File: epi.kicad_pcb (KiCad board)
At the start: 4 copper layers, 12.7 x 22.8 mm, 31 parts, among them J1 Connector 1x12, J2 Connector 1x12, J3 Conn_01x05, J4 USB-C 2.0 mid-mount female co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, U1 ATmega32U4-M, Y1 Crystal_GND24

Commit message: minor changes
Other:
- outline, holes or cut-outs redrawn
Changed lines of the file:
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@@
     )
     (pad_to_mask_clearance 0)
+    (grid_origin 108.895036 55.708644)
     (pcbplotparams
       (layerselection 0x00010fc_ffffffff)
@@
   (net 41 "D12")
   (net 42 "D13")
-  (net 43 "Net-(J4-PadA4)")
+  (net 43 "Net-(FB1-Pad1)")
   (net 44 "Net-(D2-Pad2)")
   (net 45 "Net-(F1-Pad1)")
@@
       (net 2 "GND") (pintype "passive"))
     (pad "2" smd roundrect (at 0.51 0 90) (size 0.54 0.64) (layers "F.Cu" "F.Paste" "F.Mask") (roundrect_rratio 0.25)
-      (net 43 "Net-(J4-PadA4)") (pintype "passive"))
+      (net 43 "Net-(FB1-Pad1)") (pintype "passive"))
     (model "${KICAD6_3DMODEL_DIR}/Resistor_SMD.3dshapes/R_0402_1005Metric.wrl"
       (offset (xyz 0 0 0))
@@
     (fp_line (start -0.525 -0.27) (end 0.525 -0.27) (layer "F.Fab") (width 0.1))
     (pad "1" smd roundrect (at -0.51 0 90) (size 0.54 0.64) (layers "F.Cu" "F.Paste" "F.Mask") (roundrect_rratio 0.25)
-      (net 43 "Net-(J4-PadA4)") (pintype "passive"))
+      (net 43 "Net-(FB1-Pad1)") (pintype "passive"))
     (pad "2" smd roundrect (at 0.51 0 90) (size 0.54 0.64) (layers "F.Cu" "F.Paste" "F.Mask") (roundrect_rratio 0.25)
       (net 45 "Net-(F1-Pad1)") (pintype "passive"))
@@
       (effects (font (size 1 1) (thickness 0.15)))
     )
-    (fp_rect (start 3 -4.5) (end 3.4 -3.5) (layer "F.Paste") (width 0) (fill solid))
     (pad "A1" smd rect locked (at -3.2 -4 270) (size 1 0.6155) (layers "F.Cu" "F.Paste" "F.Mask")
       (net 2 "GND") (pinfunction "GND") (pintype "passive"))
-    (pad "A1" smd rect locked (at 3.2 -4 270) (size 1 0.6155) (layers "F.Cu" "F.Mask")
+    (pad "A1" smd rect locked (at 3.2 -4 270) (size 1 0.6155) (layers "F.Cu" "F.Paste" "F.Mask")
       (net 2 "GND") (pinfunction "GND") (pintype "passive"))
     (pad "A4" smd rect locked (at -2.4 -4 270) (size 1 0.6155) (layers "F.Cu" "F.Paste" "F.Mask")
-      (net 43 "Net-(J4-PadA4)") (pinfunction "VBUS") (pintype "passive"))
+      (net 43 "Net-(FB1-Pad1)") (pinfunction "VBUS") (pintype "passive"))
     (pad "A5" smd rect locked (at -1.250923 -4 270) (size 1 0.30775) (layers "F.Cu" "F.Paste" "F.Mask")
       (net 11 "Net-(J4-PadA5)") (pinfunction "CC1") (pintype "bidirectional"))
@@
       (net 13 "Net-(J4-PadA7)") (pinfunction "D-") (pintype "bidirectional"))
     (pad "A9" smd rect locked (at 2.4 -4 270) (size 1 0.6155) (layers "F.Cu" "F.Paste" "F.Mask")
-      (net 43 "Net-(J4-PadA4)") (pinfunction "VBUS") (pintype "passive"))
+      (net 43 "Net-(FB1-Pad1)") (pinfunction "VBUS") (pintype "passive"))
     (pad "B5" smd rect locked (at 1.752189 -4 270) (size 1 0.30775) (layers "F.Cu" "F.Paste" "F.Mask")
       (net 14 "Net-(J4-PadB5)") (pinfunction "CC2") (pintype "bidirectional"))
@@
   (gr_line (start 110.69 51.4) (end 110.69 53.65) (layer "Edge.Cuts") (width 0.1))
   (gr_line (start 97.99 51.4) (end 97.99 53.65) (layer "Edge.Cuts") (width 0.1))
-  (gr_line (start 99.64 57.3365) (end 100.84 56.8365) (layer "Edge.Cuts") (width 0.1))
+  (gr_line (start 99.77322 51.4) (end 99.77322 55.708644) (layer "Edge.Cuts") (width 0.1))
   (gr_line (start 100.84 56.8365) (end 107.84 56.8365) (layer "Edge.Cuts") (width 0.1))
   (gr_arc (start 110.69 55.65) (mid 109.69 54.65) (end 110.69 53.65) (layer "Edge.Cuts") (width 0.1))
   (gr_arc (start 97.99 53.65) (mid 98.99 54.65) (end 97.99 55.65) (layer "Edge.Cuts") (width 0.1))
-  (gr_line (start 109.04 51.4) (end 110.69 51.4) (layer "Edge.Cuts") (width 0.1))
-  (gr_line (start 109.04 57.3365) (end 109.04 51.4) (layer "Edge.Cuts") (width 0.1))
+  (gr_arc (start 108.895036 55.708644) (mid 108.814317 56.690524) (end 107.84 56.8365) (layer "Edge.Cuts") (width 0.1))
+  (gr_line (start 108.895036 51.4) (end 110.69 51.4) (layer "Edge.Cuts") (width 0.1))
+  (gr_line (start 108.895036 55.708644) (end 108.895036 51.4) (layer "Edge.Cuts") (width 0.1))
   (gr_line (start 110.69 74.16) (end 110.69 55.65) (layer "Edge.Cuts") (width 0.1))
   (gr_line (start 97.99 74.16) (end 110.69 74.16) (layer "Edge.Cuts") (width 0.1))
   (gr_line (start 97.99 55.65) (end 97.99 74.16) (layer "Edge.Cuts") (width 0.1))
-  (gr_line (start 97.99 51.4) (end 99.64 51.4) (layer "Edge.Cuts") (width 0.1))
-  (gr_line (start 99.64 51.4) (end 99.64 57.3365) (layer "Edge.Cuts") (width 0.1))
-  (gr_line (start 107.84 56.8365) (end 109.04 57.3365) (layer "Edge.Cuts") (width 0.1))
+  (gr_line (start 97.99 51.4) (end 99.77322 51.4) (layer "Edge.Cuts") (width 0.1))
+  (gr_arc (start 100.828256 56.8365) (mid 99.853938 56.690524) (end 99.77322 55.708644) (layer "Edge.Cuts") (width 0.1))
   (gr_text "A1" (at 109.09 66.613) (layer "B.SilkS")
     (effects (font (size 0.8 0.8) (thickness 0.16)) (justify mirror))
@@
   (via (at 103.549883 66.991639) (size 0.6) (drill 0.2) (layers "F.Cu" "B.Cu") (net 2))
   (via (at 101.179122 69.620878) (size 0.6) (drill 0.2) (layers "F.Cu" "B.Cu") (free) (net 2))
-  (segment (start 102.34 68.319037) (end 103 67.659037) (width 0.15) (layer "F.Cu") (net 3))
+  (segment (start 103 67.659037) (end 103 66.782037) (width 0.15) (layer "F.Cu") (net 3))
+  (segment (start 104.8 65.2) (end 105.691356 64.308644) (width 0.15) (layer "F.Cu") (net 3))
+  (segment (start 105.691356 64.308644) (end 106.248706 64.308644) (width 0.15) (layer "F.Cu") (net 3))
+  (segment (start 103 66.782037) (end 103.115 66.667037) (width 0.15) (layer "F.Cu") (net 3))
+  (segment (start 108.535 63.45) (end 108.93 63.45) (width 0.15) (layer "F.Cu") (net 3))
+  (segment (start 103.115 66.667037) (end 103.115 65.445815) (width 0.15) (layer "F.Cu") (net 3))
+  (segment (start 106.87085 63.6865) (end 107.6775 63.6865) (width 0.15) (layer "F.Cu") (net 3))
   (segment (start 102.34 69.524) (end 102.34 68.319037) (width 0.15) (layer "F.Cu") (net 3))
-  (segment (start 108.535 63.45) (end 108.93 63.45) (width 0.15) (layer "F.Cu") (net 3))
-  (segment (start 104.8 65.2) (end 105.6 64.4) (width 0.15) (layer "F.Cu") (net 3))
-  (segment (start 106.87085 63.6865) (end 107.6775 63.6865) (width 0.15) (layer "F.Cu") (net 3))
-  (segment (start 105.6 64.4) (end 106.15735 64.4) (width 0.15) (layer "F.Cu") (net 3))
-  (segment (start 103 67.659037) (end 103 66.782037) (width 0.15) (layer "F.Cu") (net 3))
-  (segment (start 103 66.782037) (end 103.115 66.667037) (width 0.15) (layer "F.Cu") (net 3))
+  (segment (start 103.360815 65.2) (end 104.8 65.2) (width 0.15) (layer "F.Cu") (net 3))
+  (segment (start 103.115 65.445815) (end 103.360815 65.2) (width 0.15) (layer "F.Cu") (net 3))
   (segment (start 108.2985 63.6865) (end 108.535 63.45) (width 0.15) (layer "F.Cu") (net 3))
   (segment (start 107.6775 63.6865) (end 108.2985 63.6865) (width 0.15) (layer "F.Cu") (net 3))
   (segment (start 108.92 63.46) (end 108.93 63.45) (width 0.15) (layer "F.Cu") (net 3))
-  (segment (start 103.360815 65.2) (end 104.8 65.2) (width 0.15) (layer "F.Cu") (net 3))
-  (segment (start 103.115 66.667037) (end 103.115 65.445815) (width 0.15) (layer "F.Cu") (net 3))
-  (segment (start 106.15735 64.4) (end 106.87085 63.6865) (width 0.15) (layer "F.Cu") (net 3))
-  (segment (start 103.115 65.445815) (end 103.360815 65.2) (width 0.15) (layer "F.Cu") (net 3))
+  (segment (start 106.248706 64.308644) (end 106.87085 63.6865) (width 0.15) (layer "F.Cu") (net 3))
+  (segment (start 102.34 68.319037) (end 103 67.659037) (width 0.15) (layer "F.Cu") (net 3))
   (segment (start 108.92 64.32) (end 108.92 63.46) (width 0.15) (layer "F.Cu") (net 3))
   (segment (start 104.4 61.08) (end 103.87 60.55) (width 0.2) (layer "F.Cu") (net 4))

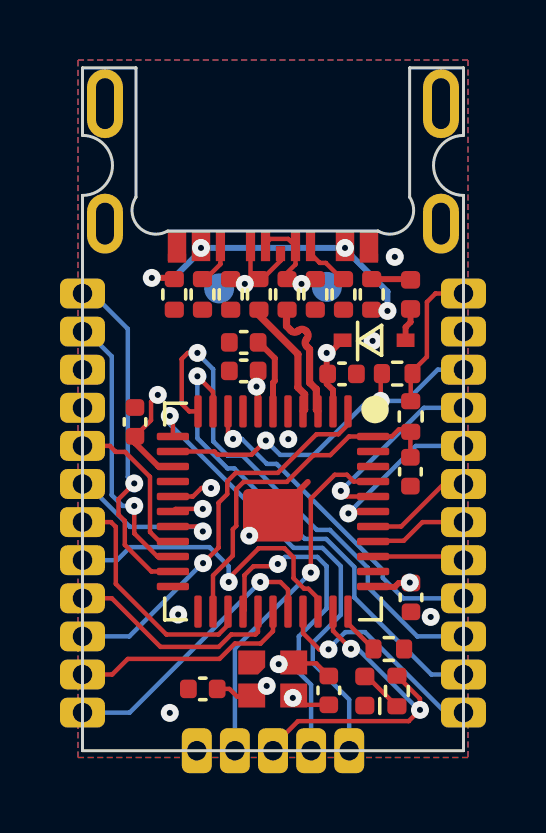
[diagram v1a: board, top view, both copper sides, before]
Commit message: minor design changes and pinout diagram added
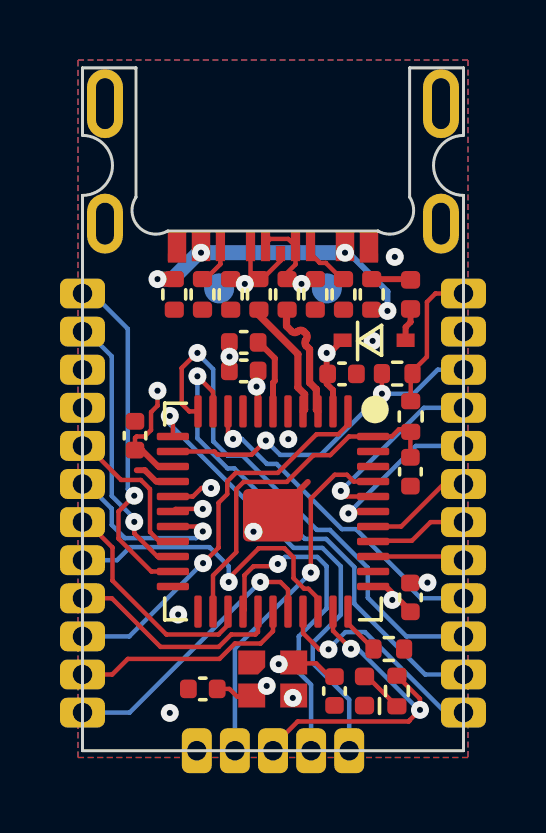
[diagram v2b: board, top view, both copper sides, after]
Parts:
- moved C9 0.46 mm to (99.7, 63.7)
- moved C5 0.19 mm to (106.4, 72.2)
- turned C3 to -90 degrees
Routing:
- net +5V: track 13.9 -> 14.6 mm
- net Net-(J4-PadA6): track 4.00 -> 4.58 mm
- net D3/SCL: track 5.73 -> 6.23 mm
- net GND: track 2.91 -> 2.98 mm, vias 8 -> 9

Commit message: new computer, new updates
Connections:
- J3 pad 4: A5 -> D17/SS
- J3 pad 5: GND -> A5
- U1 pad 8: unconnected-(U1-Pad8) -> D17/SS
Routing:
- net D17/SS: track 0.00 -> 19.0 mm, vias 0 -> 1
- net A5: track 12.0 -> 12.5 mm
- net GND: vias 9 -> 10
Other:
- outline, holes or cut-outs redrawn
- board text added: "17"

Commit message: gerbers update
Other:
- board text added: "Epi v1,2,1"
- board text removed: "Epi v1,2,0"
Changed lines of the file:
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@@
     (effects (font (size 0.8 0.8) (thickness 0.16)) (justify mirror))
   )
-  (gr_text "Epi v1,2,0" (at 104.34 60.404121) (layer "B.SilkS")
+  (gr_text "Epi v1,2,1" (at 104.34 60.404121) (layer "B.SilkS")
     (effects (font (size 1 1) (thickness 0.21)) (justify mirror))
   )
